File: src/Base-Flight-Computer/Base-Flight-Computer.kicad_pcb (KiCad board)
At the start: 4 copper layers, 43.6 x 20.3 mm, 62 parts, among them J1 Jumper_NO, P1 1984659, P2 USB, P3 0530470610, P4 1984659, P5 1984659, Q1 QS5U17TR, Q2 2N7002W-7-F, Q3 2N7002W-7-F, Q4 QS5U17TR, Q5 2N7002W-7-F, Q6 2N7002W-7-F, U1 STM32G4A1KEU6, U2 BMP390, U3 LMS8117AMP-3.3_NOPB, U4 SST25VF040B-50-4I-S2AE-T, Y1 ECS-240-18-33-JGN-TR

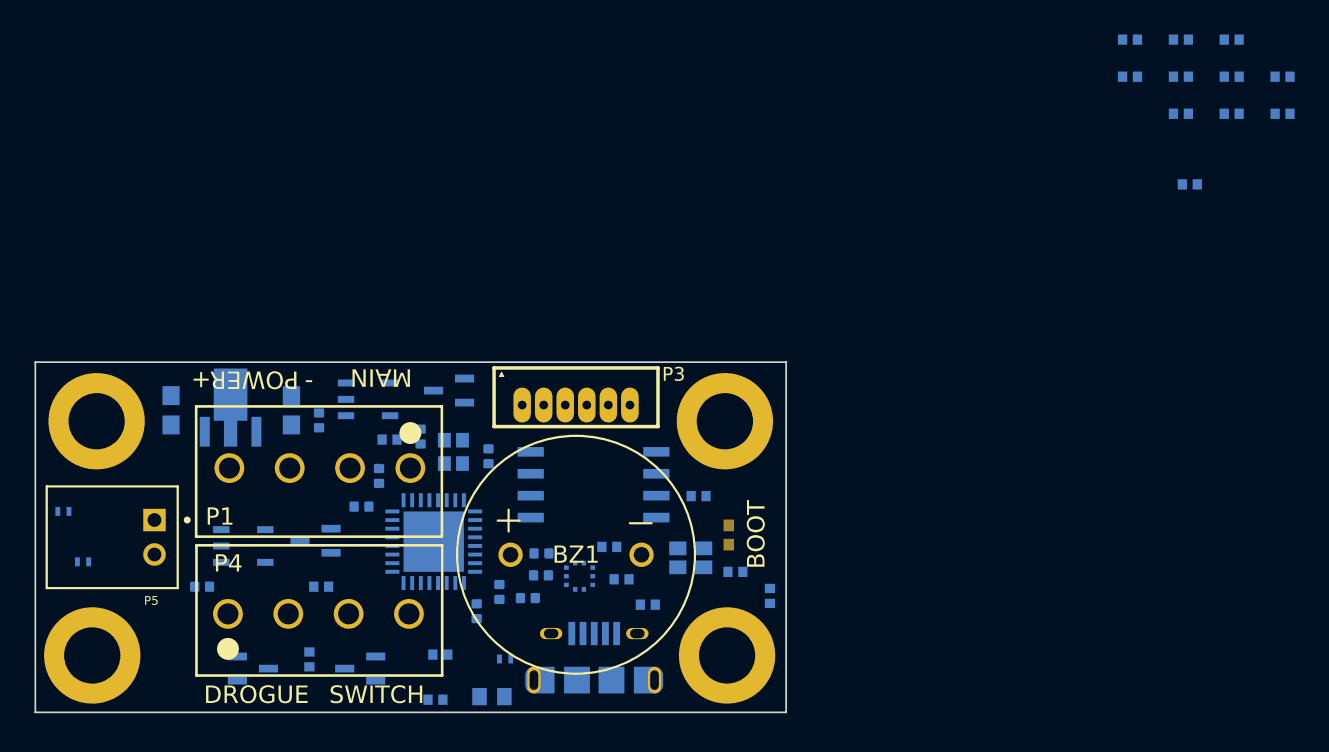
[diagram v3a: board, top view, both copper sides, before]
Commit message: swapped out 90 degree LiPo connector for straight connector
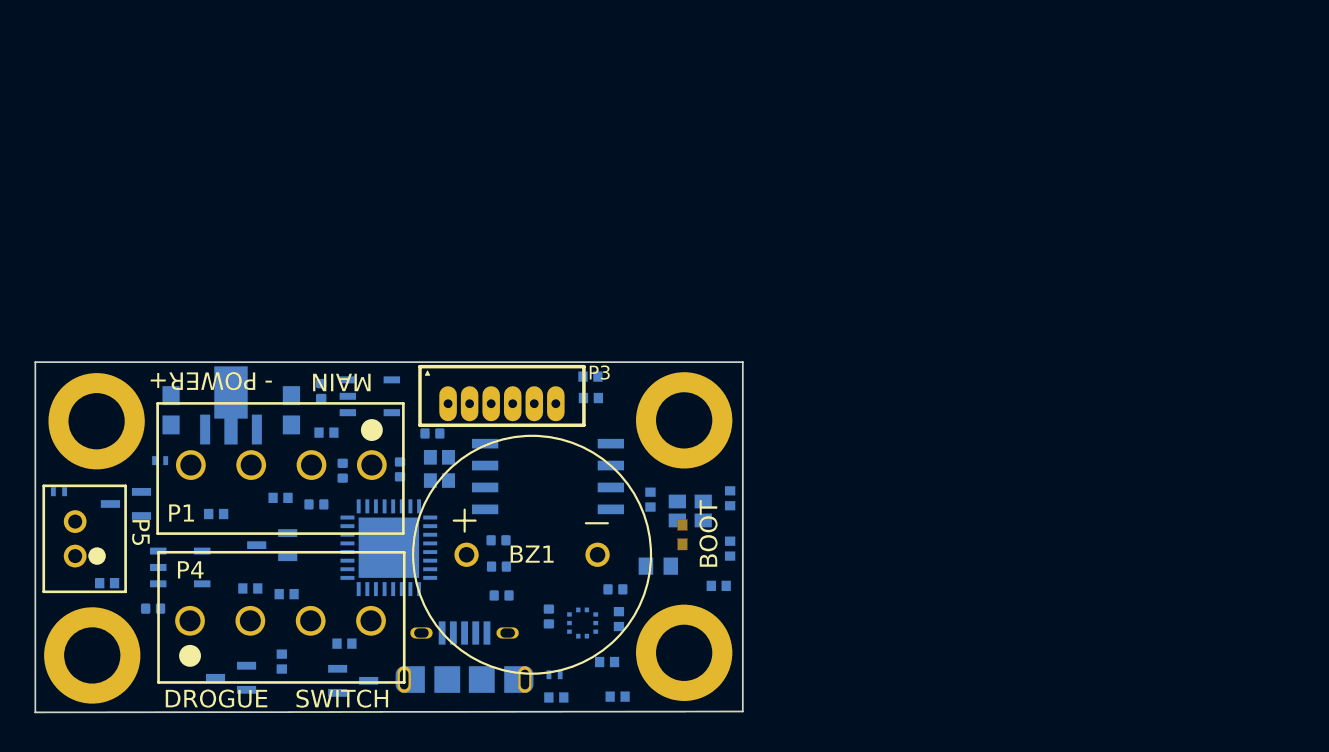
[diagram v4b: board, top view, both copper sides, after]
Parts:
- removed R10, R14, R15, R2: 100k, Base-Flight-Computer:RES_0402
- P5: value 1984659 -> B2B-PH-K-SLFSN_JST; footprint Base-Flight-Computer:JST_S2B-PH-K-S(LF)(SN) -> Base-Flight-Computer:B2B-PH-K-SLFSN_JST
- moved R22 73.4 mm to (131.2, 94.1)
- moved R21 66.9 mm to (137.5, 90.1)
- moved R9 59.9 mm to (141.6, 94.7)
- moved R3 51.0 mm to (143.9, 85.4)
- moved R8 50.2 mm to (160.8, 100.7)
- moved R16 40.4 mm to (166.6, 94.3)
- moved R17 36.9 mm to (159.2, 83.4), turned to 0 degrees
- moved Q2 19.9 mm to (132.3, 89.5)
- moved D3 12.3 mm to (163.1, 93.1)
- moved R19 9.35 mm to (159.2, 82.1)
- moved R4 8.91 mm to (162.7, 89.3), turned to 90 degrees
- moved R6 7.80 mm to (167.3, 89.2), turned to 90 degrees
- moved P2 7.52 mm to (151.9, 99.7)
- moved Q5 7.51 mm to (138.4, 99.6)
- moved D4 7.38 mm to (134.2, 87.0), turned to 0 degrees
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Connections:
- D4 pad A: Net-(P1A-5) -> Net-(P1B-6)
- P1 pad 1: Net-(P1A-5) -> VIN_SW
- P1 pad 2: Earth -> Net-(P1A-6)
- P1 pad 3: VIN_SW -> Earth
- Q1 pad 5: Net-(P1B-6) -> Net-(P1A-6)
- Q2 pad 1: Net-(P1B-6) -> Net-(P1A-6)
- R3 pad 2: Net-(P1B-6) -> Net-(P1A-6)
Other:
- board size 43.6 x 20.3 mm -> 41 x 20.3 mm
- board text added: "POW"

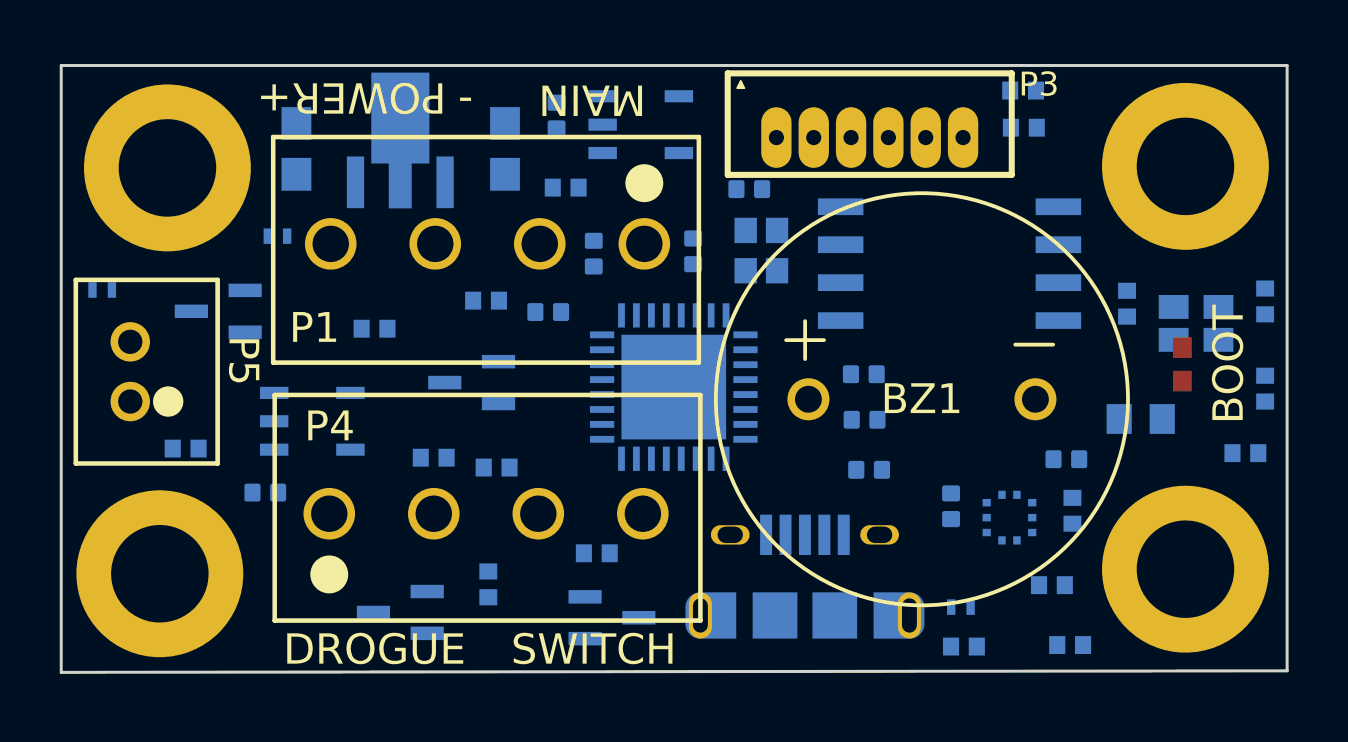
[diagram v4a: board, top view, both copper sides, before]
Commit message: finished placing components on board
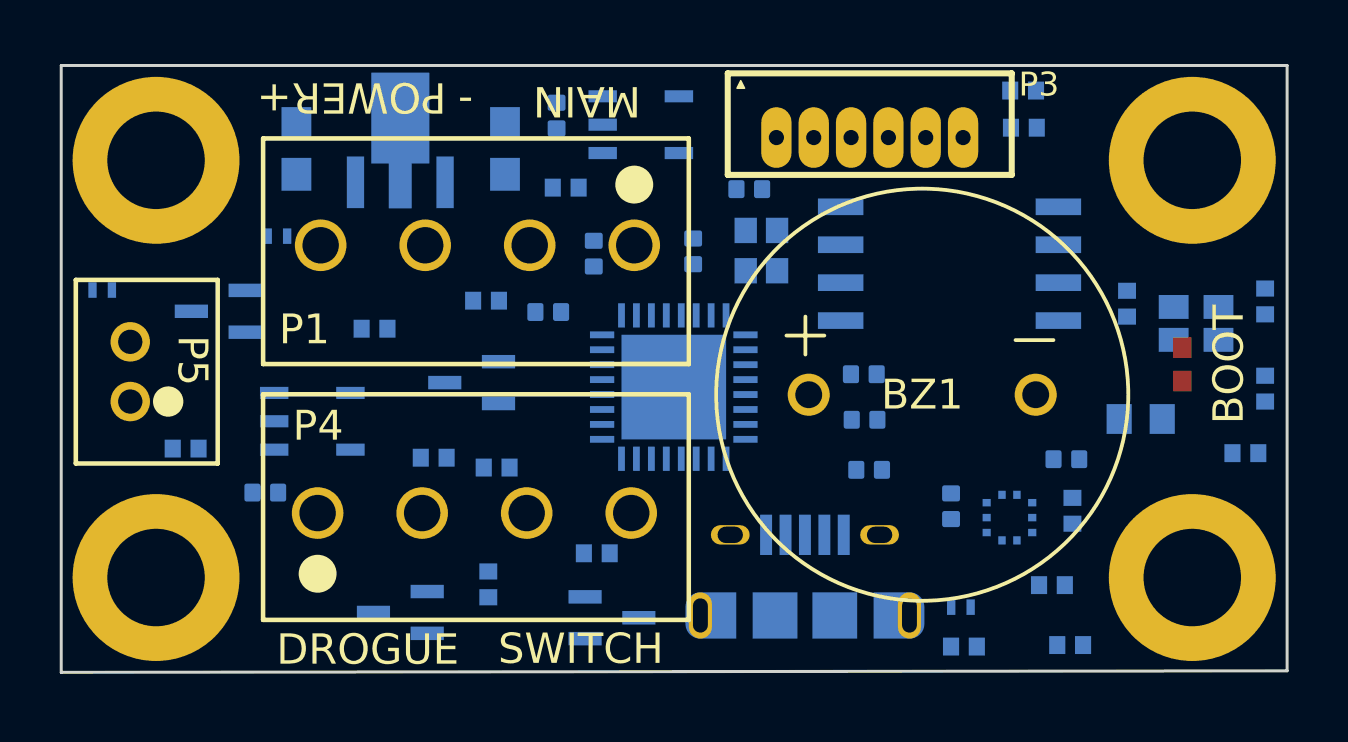
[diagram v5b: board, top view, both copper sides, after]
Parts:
- moved H2 0.46 mm to (130.2, 84.5)
- moved P4 0.39 mm to (135.6, 96.3)
- moved H3 0.36 mm to (164.9, 98.4)
- moved P1 0.34 mm to (146.2, 87.3)
- moved H1 0.31 mm to (164.9, 84.5)
- moved H4 0.18 mm to (130.2, 98.4)
- moved BZ1 0.15 mm to (155.8, 92.3)
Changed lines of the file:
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@@
   (net 49 "Net-(P1B-6)")
   (footprint "Base-Flight-Computer:MountingHole_4-40" (layer "F.Cu")
-    (at 130.302 98.298)
+    (at 130.175 98.425)
     (descr "Mounting Hole 3mm")
     (tags "mounting hole 3mm")
@@
   )
   (footprint "Base-Flight-Computer:AT-1438-TWT-R" (layer "F.Cu")
-    (at 155.819 92.456)
+    (at 155.829 92.3036)
     (property "Sheetfile" "Base-Flight-Computer.kicad_sch")
     (property "Sheetname" "")
@@
     (property "Sheetname" "")
     (attr through_hole)
-    (fp_text reference "P5" (at -1.3716 -3.7846 -90 unlocked) (layer "F.SilkS")
+    (fp_text reference "P5" (at -1.3716 -2.0828 -90 unlocked) (layer "F.SilkS")
         (effects (font (size 1 1) (thickness 0.15)))
     )
@@
   )
   (footprint "Base-Flight-Computer:MountingHole_4-40" (layer "F.Cu")
-    (at 164.6428 98.1456)
+    (at 164.8714 98.425)
     (descr "Mounting Hole 3mm")
     (tags "mounting hole 3mm")
@@
   )
   (footprint "Base-Flight-Computer:1546551-4" (layer "F.Cu")
-    (at 146.524 87.2522 180)
+    (at 146.186802 87.2998 180)
     (tags "1546551-4 ")
     (property "Sheetfile" "Base-Flight-Computer.kicad_sch")
@@
   )
   (footprint "Base-Flight-Computer:MountingHole_4-40" (layer "F.Cu")
-    (at 164.6428 84.6582)
+    (at 164.8714 84.455)
     (descr "Mounting Hole 3mm")
     (tags "mounting hole 3mm")
@@
   )
   (footprint "Base-Flight-Computer:1546551-4" (layer "F.Cu")
-    (at 135.9748 96.288201)
+    (at 135.5852 96.266)
     (tags "1546551-4 ")
     (property "Sheetfile" "Base-Flight-Computer.kicad_sch")
@@
   )
   (footprint "Base-Flight-Computer:MountingHole_4-40" (layer "F.Cu")
-    (at 130.556 84.709)
+    (at 130.175 84.455)
     (descr "Mounting Hole 3mm")
     (tags "mounting hole 3mm")
@@
     (effects (font (size 0.762 0.762) (thickness 0.127) bold) (justify mirror))
   )
-  (gr_text "DROGUE" (at 137.4902 100.838) (layer "F.SilkS")
+  (gr_text "DROGUE" (at 137.2616 100.838) (layer "F.SilkS")
     (effects (font (size 1.016 1.016) (thickness 0.2032)))
   )
-  (gr_text "MAIN" (at 144.78 82.423 180) (layer "F.SilkS")
+  (gr_text "MAIN" (at 144.6022 82.4738 180) (layer "F.SilkS")
     (effects (font (size 1.016 1.016) (thickness 0.2032)))
   )
-  (gr_text "SWITCH" (at 144.8308 100.838) (layer "F.SilkS")
+  (gr_text "SWITCH" (at 144.399 100.8126) (layer "F.SilkS")
     (effects (font (size 1.016 1.016) (thickness 0.2032)))
   )

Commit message: created new project for preliminary hardware testing
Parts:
- moved C10 4.52 mm to (149.3, 83.1), turned to -90 degrees
- moved C1 2.37 mm to (151.6, 93.8)
- moved C4 1.99 mm to (153.9, 92.8)
- moved C11 1.26 mm to (148.8, 85.6), turned to 90 degrees
- moved Y1 1.04 mm to (150.6, 86.5), turned to -90 degrees
- moved P1 0.58 mm to (146.2, 86.7)
- moved U1 0.50 mm to (147.4, 91.6)
- moved D4 0.46 mm to (133.8, 87.0)
- moved U3 0.45 mm to (138.0, 83.8), turned to 180 degrees
- moved Q2 0.39 mm to (132.2, 89.9)
- moved C2 0.38 mm to (144.5, 87.5)
- moved C3 0.33 mm to (143.3, 89.2)
- moved P2 0.27 mm to (151.8, 100.0)
- moved Q1 0.24 mm to (146.2, 83.1)
- moved C13 0.19 mm to (141.8, 83.9), turned to -90 degrees
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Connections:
- U1 pad 30: STATUS_B -> ~{MAIN_CONT}
- U1 pad 33: unconnected-(U1-Exposed_Pad-Pad33) -> Earth
- U1 pad 9: ~{MAIN_CONT} -> STATUS_B
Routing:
- net VIN: track 0.00 -> 61.0 mm, vias 0 -> 3
- net Earth: track 0.00 -> 18.0 mm, vias 0 -> 11
- net 3.3V: track 0.00 -> 15.5 mm, vias 0 -> 3
- net OSC_IN: track 0.00 -> 12.8 mm, vias 0 -> 2
- net USB_D-: track 0.00 -> 8.48 mm
- net USB_D+: track 0.00 -> 8.22 mm
- net OSC_OUT: track 0.00 -> 6.03 mm
- net 5V: track 0.00 -> 4.80 mm
- net USB_DETECT: track 0.00 -> 4.27 mm
- net ~{SWITCH}: track 0.00 -> 3.60 mm
- net BP_SCL: track 0.00 -> 3.03 mm
- net BEEP: track 0.00 -> 2.91 mm
- net STATUS_G: track 0.00 -> 2.75 mm, vias 0 -> 1
- net NRST: track 0.00 -> 2.53 mm, vias 0 -> 1
- net VBAT_SENSE: track 0.00 -> 2.37 mm, vias 0 -> 1
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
